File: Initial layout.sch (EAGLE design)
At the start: 51 parts, among them J1 502585-0470, U2 TPS54540DDARQ1

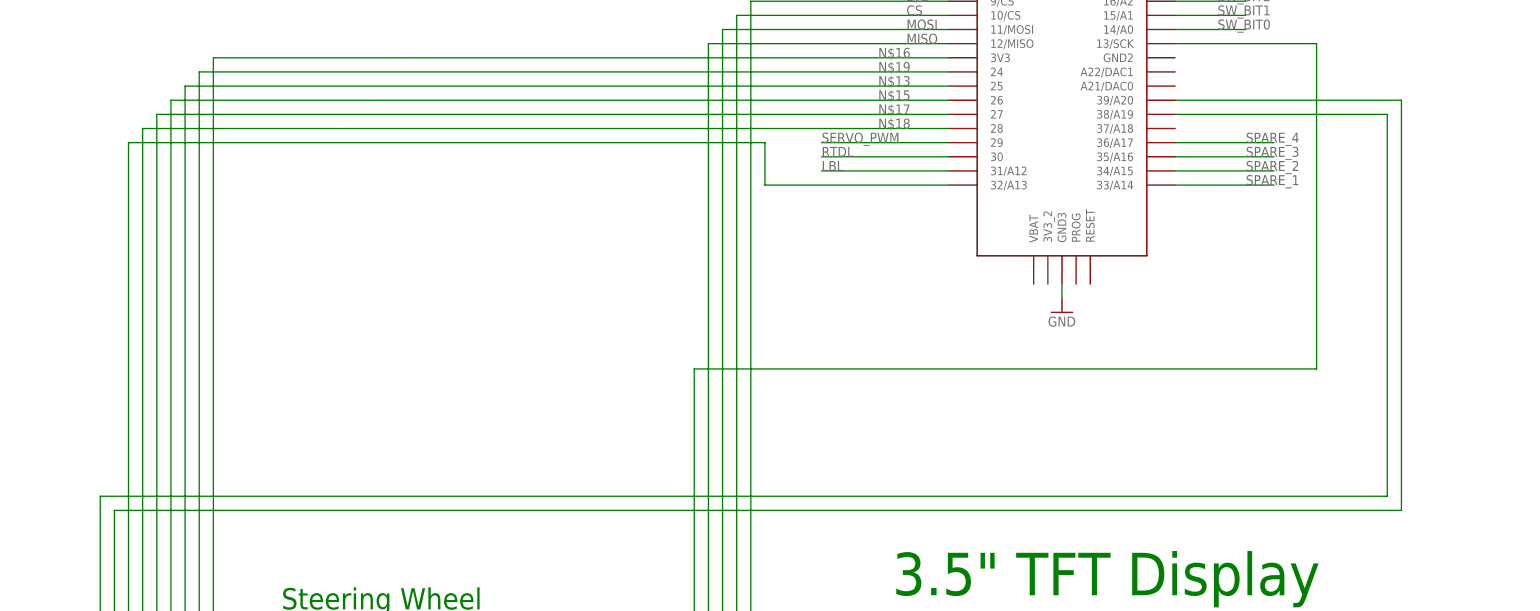
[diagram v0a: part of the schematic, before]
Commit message: Added resistors for LEDs
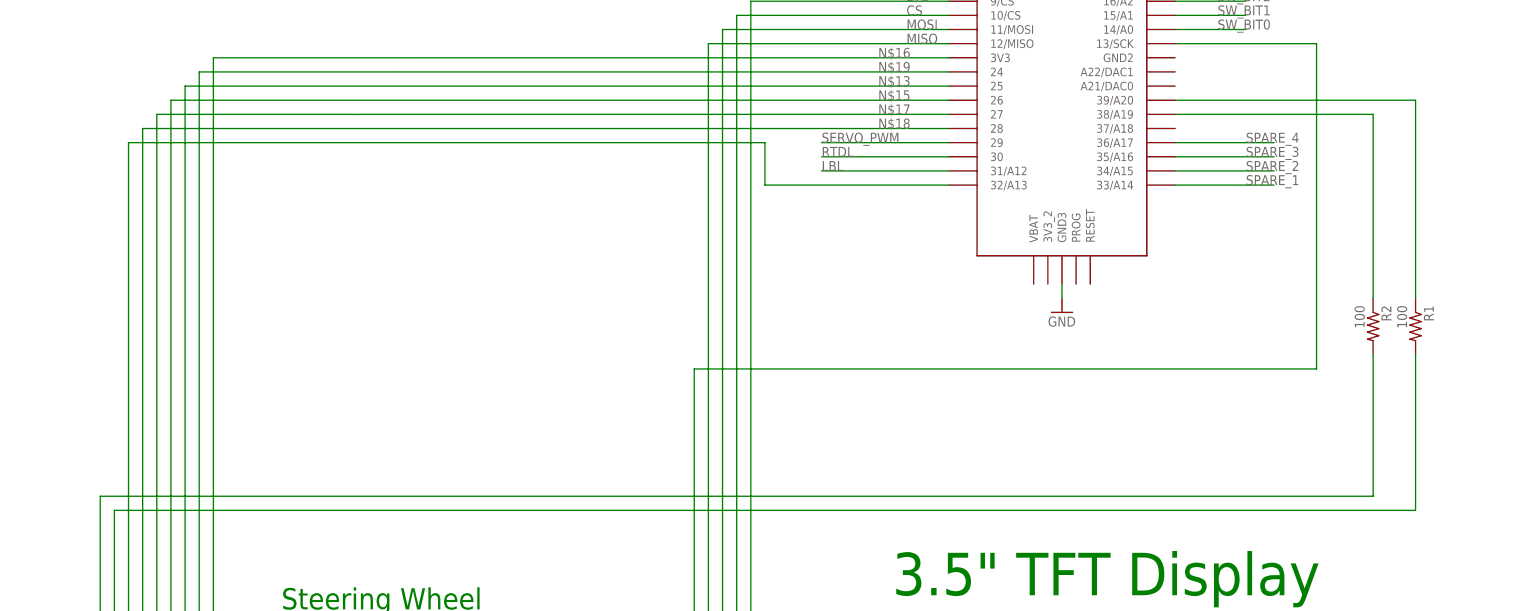
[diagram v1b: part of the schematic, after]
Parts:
- added R1, R2: 100, rcl:R-US_R0805
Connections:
- new net N$41: R1.1, U$2.39/A20
- new net N$42: R2.1, U$2.38/A19
- net N$34: now also R2.2; no longer U$2.38/A19
- net N$35: now also R1.2; no longer U$2.39/A20
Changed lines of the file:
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@@
 <part name="J1" library="FormE" deviceset="MOLEX_CLICKMATE-4-R/A" device="" value="502585-0470"/>
 <part name="GND23" library="supply1" deviceset="GND" device=""/>
+<part name="R1" library="rcl" deviceset="R-US_" device="R0805" value="100"/>
+<part name="R2" library="rcl" deviceset="R-US_" device="R0805" value="100"/>
 </parts>
 <sheets>
@@
 <instance part="J1" gate="G$1" x="132.08" y="-426.72"/>
 <instance part="GND23" gate="1" x="121.92" y="-436.88"/>
+<instance part="R1" gate="G$1" x="317.5" y="-307.34" rot="R270"/>
+<instance part="R2" gate="G$1" x="309.88" y="-307.34" rot="R270"/>
 </instances>
 <busses>
@@
 <wire x1="129.54" y1="-421.64" x2="81.28" y2="-421.64" width="0.1524" layer="91"/>
 <wire x1="81.28" y1="-421.64" x2="81.28" y2="-337.82" width="0.1524" layer="91"/>
-<wire x1="81.28" y1="-337.82" x2="312.42" y2="-337.82" width="0.1524" layer="91"/>
-<pinref part="U$2" gate="G$1" pin="38/A19"/>
-<wire x1="312.42" y1="-337.82" x2="312.42" y2="-269.24" width="0.1524" layer="91"/>
-<wire x1="312.42" y1="-269.24" x2="274.32" y2="-269.24" width="0.1524" layer="91"/>
+<wire x1="81.28" y1="-337.82" x2="309.88" y2="-337.82" width="0.1524" layer="91"/>
+<wire x1="309.88" y1="-337.82" x2="309.88" y2="-312.42" width="0.1524" layer="91"/>
+<pinref part="R2" gate="G$1" pin="2"/>
 </segment>
 </net>
@@
 <wire x1="129.54" y1="-424.18" x2="83.82" y2="-424.18" width="0.1524" layer="91"/>
 <wire x1="83.82" y1="-424.18" x2="83.82" y2="-340.36" width="0.1524" layer="91"/>
-<wire x1="83.82" y1="-340.36" x2="314.96" y2="-340.36" width="0.1524" layer="91"/>
+<wire x1="83.82" y1="-340.36" x2="317.5" y2="-340.36" width="0.1524" layer="91"/>
+<wire x1="317.5" y1="-340.36" x2="317.5" y2="-312.42" width="0.1524" layer="91"/>
+<pinref part="R1" gate="G$1" pin="2"/>
+</segment>
+</net>
+<net name="N$41" class="0">
+<segment>
 <pinref part="U$2" gate="G$1" pin="39/A20"/>
-<wire x1="314.96" y1="-340.36" x2="314.96" y2="-266.7" width="0.1524" layer="91"/>
-<wire x1="314.96" y1="-266.7" x2="274.32" y2="-266.7" width="0.1524" layer="91"/>
-</segment>
-</net>
+<pinref part="R1" gate="G$1" pin="1"/>
+<wire x1="317.5" y1="-302.26" x2="317.5" y2="-266.7" width="0.1524" layer="91"/>
+<wire x1="317.5" y1="-266.7" x2="274.32" y2="-266.7" width="0.1524" layer="91"/>
+</segment>
+</net>
+<net name="N$42" class="0">
+<segment>
+<pinref part="U$2" gate="G$1" pin="38/A19"/>
+<pinref part="R2" gate="G$1" pin="1"/>
+<wire x1="309.88" y1="-302.26" x2="309.88" y2="-269.24" width="0.1524" layer="91"/>
+<wire x1="309.88" y1="-269.24" x2="274.32" y2="-269.24" width="0.1524" layer="91"/>
+</segment>
+</net>

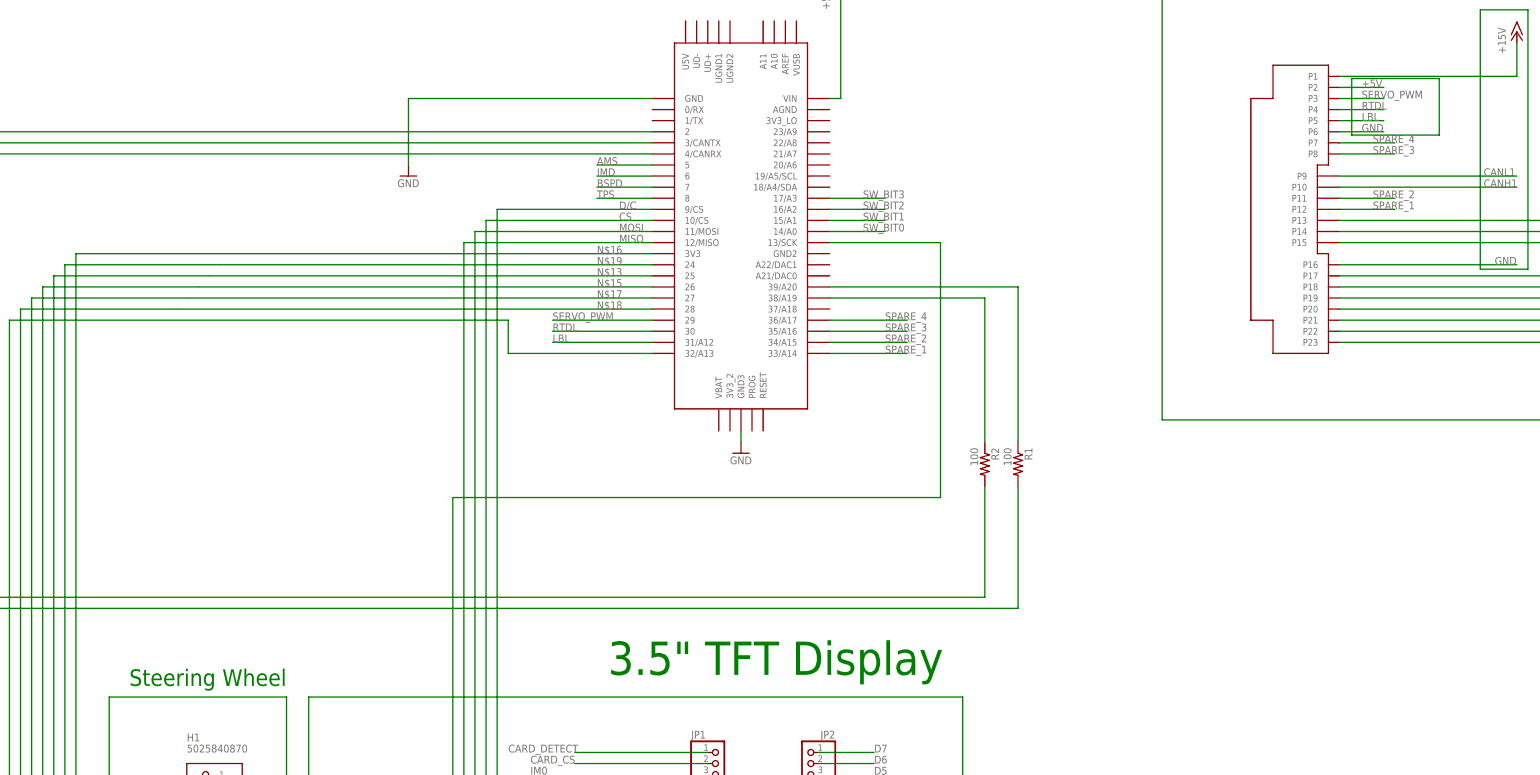
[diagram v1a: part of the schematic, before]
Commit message: Created Right Ear Board and made adjustments to Dash
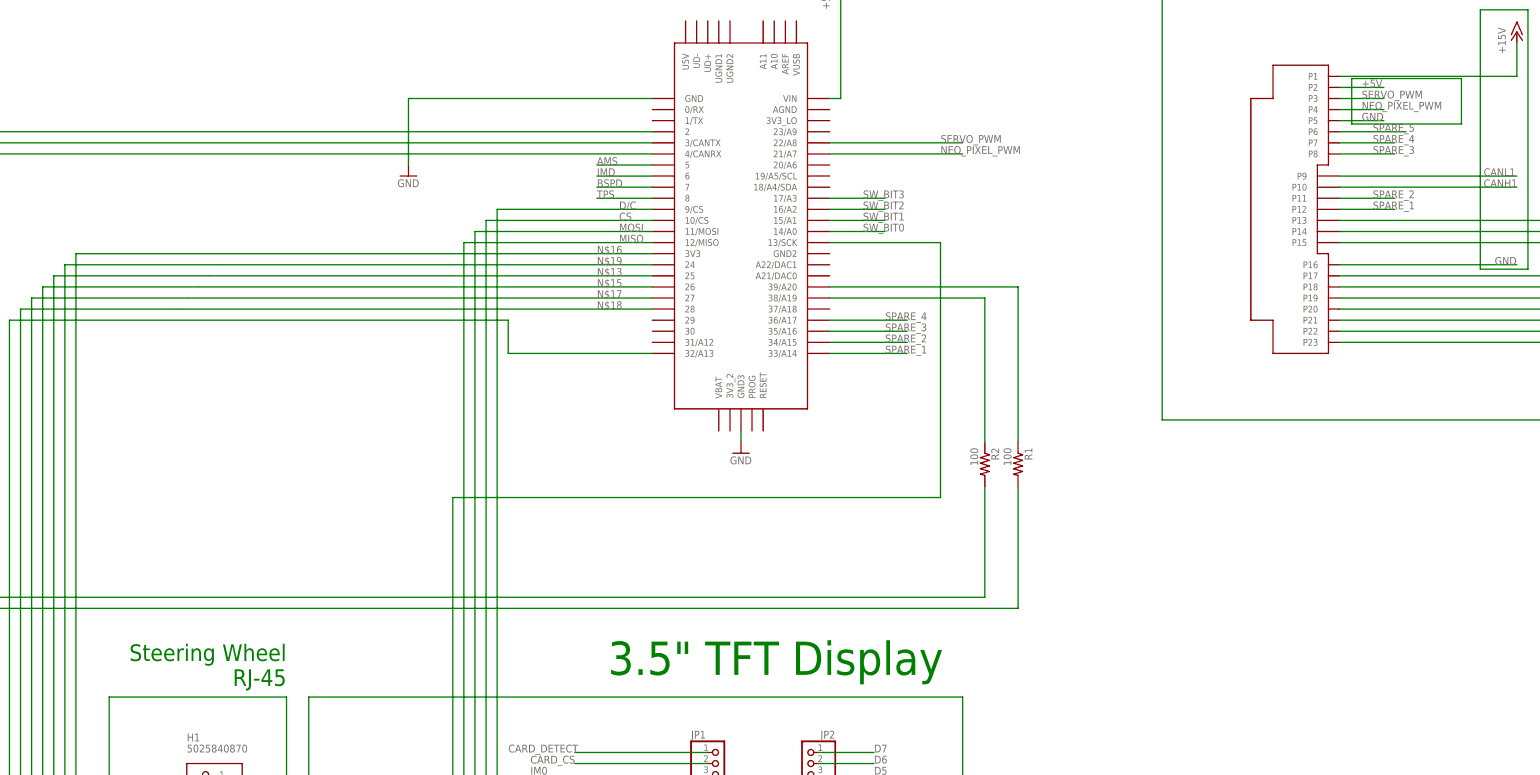
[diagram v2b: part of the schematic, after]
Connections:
- removed net LBL: U$1.P5, U$2.31/A12
- removed net RTDL: U$1.P4, U$2.30
- new net NEO_PIXEL_PWM: U$1.P4, U$2.21/A7
- new net SPARE_5: U$1.P6
- net GND: now also U$1.P5; no longer U$1.P6
- net SERVO_PWM: now also U$2.22/A8; no longer U$2.29
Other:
- note added: "Steering Wheel RJ-45"
- note removed: "Steering Wheel"
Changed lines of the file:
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@@
 <plain>
 <text x="391.16" y="-83.82" size="1.778" layer="91">7443251000</text>
-<text x="149.86" y="-358.14" size="3.81" layer="91" rot="MR0">Steering Wheel</text>
+<text x="149.86" y="-358.14" size="3.81" layer="91" rot="MR0">Steering Wheel
+        RJ-45</text>
 <text x="81.28" y="-45.72" size="7.62" layer="91">Multi-function LED Display</text>
 <text x="223.52" y="-355.6" size="7.62" layer="91">3.5" TFT Display</text>
@@
 </segment>
 <segment>
-<pinref part="U$1" gate="G$1" pin="P6"/>
-<wire x1="391.16" y1="-231.14" x2="401.32" y2="-231.14" width="0.1524" layer="91"/>
-<label x="396.24" y="-231.14" size="1.778" layer="95"/>
-</segment>
-<segment>
 <pinref part="J1" gate="G$1" pin="3"/>
 <wire x1="129.54" y1="-426.72" x2="121.92" y2="-426.72" width="0.1524" layer="91"/>
@@
 <junction x="121.92" y="-429.26"/>
 <pinref part="GND23" gate="1" pin="GND"/>
+</segment>
+<segment>
+<pinref part="U$1" gate="G$1" pin="P5"/>
+<wire x1="391.16" y1="-228.6" x2="401.32" y2="-228.6" width="0.1524" layer="91"/>
+<label x="396.24" y="-228.6" size="1.778" layer="95"/>
 </segment>
 </net>
@@
 <net name="SERVO_PWM" class="0">
 <segment>
-<pinref part="U$2" gate="G$1" pin="29"/>
-<wire x1="233.68" y1="-274.32" x2="210.82" y2="-274.32" width="0.1524" layer="91"/>
-<label x="210.82" y="-274.32" size="1.778" layer="95"/>
-</segment>
-<segment>
 <pinref part="U$1" gate="G$1" pin="P3"/>
 <wire x1="391.16" y1="-223.52" x2="401.32" y2="-223.52" width="0.1524" layer="91"/>
 <label x="396.24" y="-223.52" size="1.778" layer="95"/>
+</segment>
+<segment>
+<pinref part="U$2" gate="G$1" pin="22/A8"/>
+<wire x1="274.32" y1="-233.68" x2="304.8" y2="-233.68" width="0.1524" layer="91"/>
+<label x="299.72" y="-233.68" size="1.778" layer="95"/>
 </segment>
 </net>
@@
 </segment>
 </net>
-<net name="RTDL" class="0">
-<segment>
-<pinref part="U$1" gate="G$1" pin="P4"/>
-<wire x1="391.16" y1="-226.06" x2="401.32" y2="-226.06" width="0.1524" layer="91"/>
-<label x="396.24" y="-226.06" size="1.778" layer="95"/>
-</segment>
-<segment>
-<pinref part="U$2" gate="G$1" pin="30"/>
-<wire x1="233.68" y1="-276.86" x2="210.82" y2="-276.86" width="0.1524" layer="91"/>
-<label x="210.82" y="-276.86" size="1.778" layer="95"/>
-</segment>
-</net>
-<net name="LBL" class="0">
-<segment>
-<pinref part="U$1" gate="G$1" pin="P5"/>
-<wire x1="391.16" y1="-228.6" x2="401.32" y2="-228.6" width="0.1524" layer="91"/>
-<label x="396.24" y="-228.6" size="1.778" layer="95"/>
-</segment>
-<segment>
-<pinref part="U$2" gate="G$1" pin="31/A12"/>
-<wire x1="233.68" y1="-279.4" x2="210.82" y2="-279.4" width="0.1524" layer="91"/>
-<label x="210.82" y="-279.4" size="1.778" layer="95"/>
-</segment>
-</net>
 <net name="N$32" class="0">
 <segment>
-<wire x1="414.02" y1="-231.902" x2="414.02" y2="-218.948" width="0.1524" layer="91"/>
-<wire x1="393.954" y1="-218.948" x2="393.954" y2="-231.902" width="0.1524" layer="91"/>
-<wire x1="393.954" y1="-231.902" x2="414.02" y2="-231.902" width="0.1524" layer="91"/>
-<wire x1="393.954" y1="-218.948" x2="414.02" y2="-218.948" width="0.1524" layer="91"/>
+<wire x1="419.1" y1="-229.362" x2="419.1" y2="-218.948" width="0.1524" layer="91"/>
+<wire x1="393.954" y1="-218.948" x2="393.954" y2="-229.362" width="0.1524" layer="91"/>
+<wire x1="393.954" y1="-229.362" x2="419.1" y2="-229.362" width="0.1524" layer="91"/>
+<wire x1="393.954" y1="-218.948" x2="419.1" y2="-218.948" width="0.1524" layer="91"/>
 </segment>
 </net>
@@
 </segment>
 </net>
+<net name="NEO_PIXEL_PWM" class="0">
+<segment>
+<pinref part="U$1" gate="G$1" pin="P4"/>
+<wire x1="391.16" y1="-226.06" x2="401.32" y2="-226.06" width="0.1524" layer="91"/>
+<label x="396.24" y="-226.06" size="1.778" layer="95"/>
+</segment>
+<segment>
+<pinref part="U$2" gate="G$1" pin="21/A7"/>
+<wire x1="274.32" y1="-236.22" x2="304.8" y2="-236.22" width="0.1524" layer="91"/>
+<label x="299.72" y="-236.22" size="1.778" layer="95"/>
+</segment>
+</net>
+<net name="SPARE_5" class="0">
+<segment>
+<pinref part="U$1" gate="G$1" pin="P6"/>
+<wire x1="391.16" y1="-231.14" x2="406.4" y2="-231.14" width="0.1524" layer="91"/>
+<label x="398.78" y="-231.14" size="1.778" layer="95"/>
+</segment>
+</net>
